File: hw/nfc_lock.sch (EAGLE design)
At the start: 10 parts, among them IC1 STM8S003F3, IC3 MCP170312MB, U1 M24SR16-YMN6T/2, X1 MINI-USB-32005-301

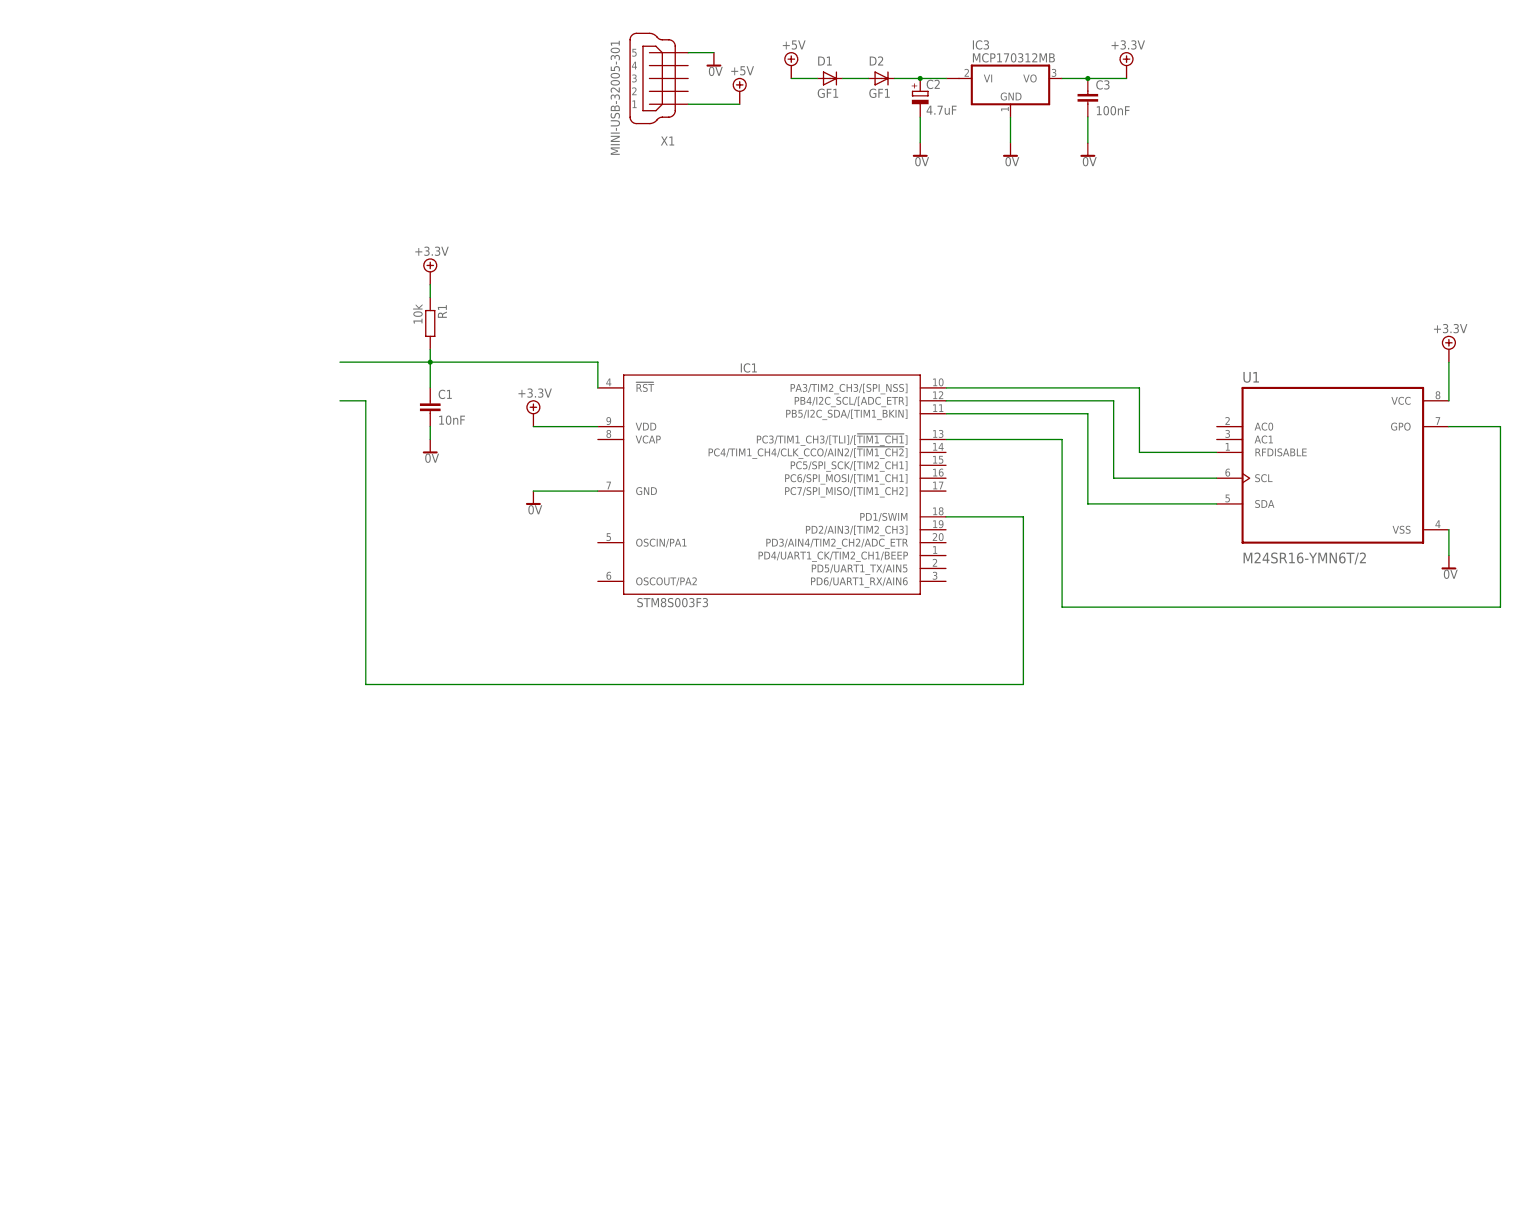
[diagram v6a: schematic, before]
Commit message: 2x n-mosfet for PWM of servos
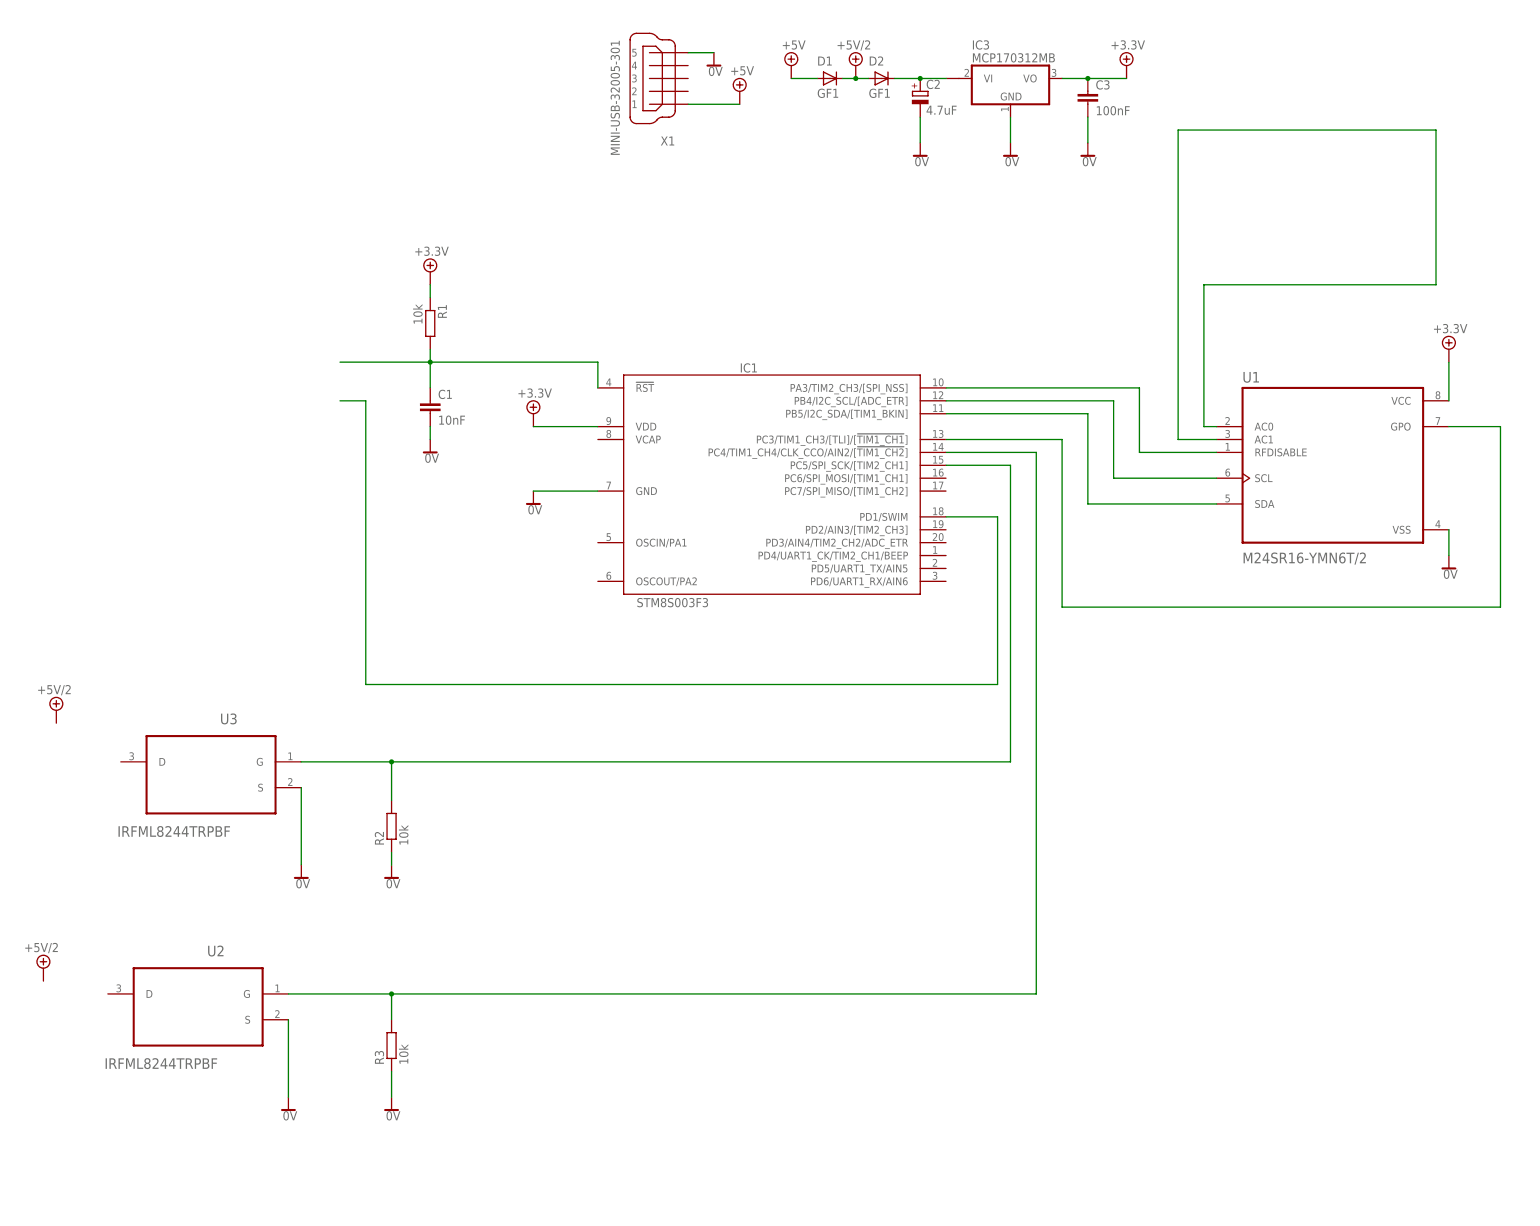
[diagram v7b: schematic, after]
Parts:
- added R2, R3: 10k, rcl:R-EU_R0805
- added U2, U3: IRFML8244TRPBF, irfml8244trpbf:IRFML8244TRPBF
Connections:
- net N$3 renamed +5V/2
- new net N$10: U1.AC0, U1.AC1
- new net N$13: IC1.PC5/SPI_SCK/[TIM2_CH1], R2.2, U3.G
- new net N$3: IC1.PC4/TIM1_CH4/CLK_CCO/AIN2/[!TIM1_CH2!], R3.2, U2.G
- net 0V: now also R2.1, R3.1, U2.S, U3.S
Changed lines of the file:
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@@
 <part name="SUPPLY12" library="supply2" deviceset="+5V/1" device="" value="+3.3V"/>
 <part name="SUPPLY13" library="supply2" deviceset="0V" device=""/>
+<part name="U3" library="irfml8244trpbf" deviceset="IRFML8244TRPBF" device=""/>
+<part name="SUPPLY14" library="supply2" deviceset="0V" device=""/>
+<part name="SUPPLY15" library="supply2" deviceset="+5V/2" device=""/>
+<part name="SUPPLY16" library="supply2" deviceset="+5V/2" device=""/>
+<part name="R2" library="rcl" deviceset="R-EU_" device="R0805" value="10k"/>
+<part name="SUPPLY17" library="supply2" deviceset="0V" device=""/>
+<part name="U2" library="irfml8244trpbf" deviceset="IRFML8244TRPBF" device=""/>
+<part name="R3" library="rcl" deviceset="R-EU_" device="R0805" value="10k"/>
+<part name="SUPPLY18" library="supply2" deviceset="0V" device=""/>
+<part name="SUPPLY19" library="supply2" deviceset="0V" device=""/>
+<part name="SUPPLY20" library="supply2" deviceset="+5V/2" device=""/>
 </parts>
 <sheets>
@@
 <instance part="SUPPLY12" gate="G$1" x="-43.18" y="116.84"/>
 <instance part="SUPPLY13" gate="0V" x="-43.18" y="81.28"/>
+<instance part="U3" gate="A" x="-86.36" y="20.32" rot="MR0"/>
+<instance part="SUPPLY14" gate="0V" x="-68.58" y="-2.54"/>
+<instance part="SUPPLY15" gate="G$1" x="40.64" y="157.48"/>
+<instance part="SUPPLY16" gate="G$1" x="-116.84" y="30.48"/>
+<instance part="R2" gate="G$1" x="-50.8" y="7.62" rot="R90"/>
+<instance part="SUPPLY17" gate="0V" x="-50.8" y="-2.54"/>
+<instance part="U2" gate="A" x="-88.9" y="-25.4" rot="MR0"/>
+<instance part="R3" gate="G$1" x="-50.8" y="-35.56" rot="R90"/>
+<instance part="SUPPLY18" gate="0V" x="-71.12" y="-48.26"/>
+<instance part="SUPPLY19" gate="0V" x="-50.8" y="-48.26"/>
+<instance part="SUPPLY20" gate="G$1" x="-119.38" y="-20.32"/>
 </instances>
 <busses>
@@
 <pinref part="SUPPLY13" gate="0V" pin="0V"/>
 <wire x1="-43.18" y1="83.82" x2="-43.18" y2="86.36" width="0.1524" layer="91"/>
+</segment>
+<segment>
+<pinref part="U3" gate="A" pin="S"/>
+<pinref part="SUPPLY14" gate="0V" pin="0V"/>
+<wire x1="-68.58" y1="15.24" x2="-68.58" y2="0" width="0.1524" layer="91"/>
+</segment>
+<segment>
+<pinref part="R2" gate="G$1" pin="1"/>
+<pinref part="SUPPLY17" gate="0V" pin="0V"/>
+<wire x1="-50.8" y1="2.54" x2="-50.8" y2="0" width="0.1524" layer="91"/>
+</segment>
+<segment>
+<pinref part="U2" gate="A" pin="S"/>
+<pinref part="SUPPLY18" gate="0V" pin="0V"/>
+<wire x1="-71.12" y1="-45.72" x2="-71.12" y2="-30.48" width="0.1524" layer="91"/>
+</segment>
+<segment>
+<pinref part="R3" gate="G$1" pin="1"/>
+<pinref part="SUPPLY19" gate="0V" pin="0V"/>
+<wire x1="-50.8" y1="-45.72" x2="-50.8" y2="-40.64" width="0.1524" layer="91"/>
 </segment>
 </net>
@@
 <pinref part="SUPPLY7" gate="+5V" pin="+5V"/>
 <wire x1="17.78" y1="149.86" x2="7.62" y2="149.86" width="0.1524" layer="91"/>
-</segment>
-</net>
-<net name="N$3" class="0">
-<segment>
-<pinref part="D1" gate="D" pin="C"/>
-<pinref part="D2" gate="D" pin="A"/>
-<wire x1="43.18" y1="154.94" x2="38.1" y2="154.94" width="0.1524" layer="91"/>
 </segment>
 </net>
@@
 <segment>
 <pinref part="IC1" gate="G$1" pin="PD1/SWIM"/>
-<wire x1="58.42" y1="68.58" x2="73.66" y2="68.58" width="0.1524" layer="91"/>
-<wire x1="73.66" y1="68.58" x2="73.66" y2="35.56" width="0.1524" layer="91"/>
-<wire x1="73.66" y1="35.56" x2="-55.88" y2="35.56" width="0.1524" layer="91"/>
+<wire x1="58.42" y1="68.58" x2="68.58" y2="68.58" width="0.1524" layer="91"/>
+<wire x1="68.58" y1="68.58" x2="68.58" y2="35.56" width="0.1524" layer="91"/>
+<wire x1="68.58" y1="35.56" x2="-55.88" y2="35.56" width="0.1524" layer="91"/>
 <wire x1="-55.88" y1="35.56" x2="-55.88" y2="91.44" width="0.1524" layer="91"/>
 <wire x1="-55.88" y1="91.44" x2="-60.96" y2="91.44" width="0.1524" layer="91"/>
@@
 </segment>
 </net>
+<net name="+5V/2" class="0">
+<segment>
+<pinref part="D1" gate="D" pin="C"/>
+<pinref part="D2" gate="D" pin="A"/>
+<wire x1="43.18" y1="154.94" x2="40.64" y2="154.94" width="0.1524" layer="91"/>
+<pinref part="SUPPLY15" gate="G$1" pin="+5V/2"/>
+<wire x1="40.64" y1="154.94" x2="38.1" y2="154.94" width="0.1524" layer="91"/>
+<junction x="40.64" y="154.94"/>
+</segment>
+</net>
+<net name="N$3" class="0">
+<segment>
+<pinref part="IC1" gate="G$1" pin="PC4/TIM1_CH4/CLK_CCO/AIN2/[!TIM1_CH2!]"/>
+<wire x1="58.42" y1="81.28" x2="76.2" y2="81.28" width="0.1524" layer="91"/>
+<wire x1="76.2" y1="81.28" x2="76.2" y2="-25.4" width="0.1524" layer="91"/>
+<pinref part="U2" gate="A" pin="G"/>
+<pinref part="R3" gate="G$1" pin="2"/>
+<wire x1="-50.8" y1="-30.48" x2="-50.8" y2="-25.4" width="0.1524" layer="91"/>
+<wire x1="-50.8" y1="-25.4" x2="-71.12" y2="-25.4" width="0.1524" layer="91"/>
+<wire x1="76.2" y1="-25.4" x2="-50.8" y2="-25.4" width="0.1524" layer="91"/>
+<junction x="-50.8" y="-25.4"/>
+</segment>
+</net>
+<net name="N$10" class="0">
+<segment>
+<pinref part="U1" gate="G$1" pin="AC1"/>
+<wire x1="111.76" y1="83.82" x2="104.14" y2="83.82" width="0.1524" layer="91"/>
+<wire x1="104.14" y1="83.82" x2="104.14" y2="144.78" width="0.1524" layer="91"/>
+<wire x1="104.14" y1="144.78" x2="154.94" y2="144.78" width="0.1524" layer="91"/>
+<wire x1="154.94" y1="144.78" x2="154.94" y2="114.3" width="0.1524" layer="91"/>
+<wire x1="154.94" y1="114.3" x2="109.22" y2="114.3" width="0.1524" layer="91"/>
+<wire x1="109.22" y1="114.3" x2="109.22" y2="86.36" width="0.1524" layer="91"/>
+<pinref part="U1" gate="G$1" pin="AC0"/>
+<wire x1="109.22" y1="86.36" x2="111.76" y2="86.36" width="0.1524" layer="91"/>
+</segment>
+</net>
+<net name="N$13" class="0">
+<segment>
+<pinref part="U3" gate="A" pin="G"/>
+<pinref part="R2" gate="G$1" pin="2"/>
+<wire x1="-50.8" y1="12.7" x2="-50.8" y2="20.32" width="0.1524" layer="91"/>
+<wire x1="-50.8" y1="20.32" x2="-68.58" y2="20.32" width="0.1524" layer="91"/>
+<pinref part="IC1" gate="G$1" pin="PC5/SPI_SCK/[TIM2_CH1]"/>
+<wire x1="58.42" y1="78.74" x2="71.12" y2="78.74" width="0.1524" layer="91"/>
+<wire x1="71.12" y1="78.74" x2="71.12" y2="20.32" width="0.1524" layer="91"/>
+<wire x1="-50.8" y1="20.32" x2="71.12" y2="20.32" width="0.1524" layer="91"/>
+<junction x="-50.8" y="20.32"/>
+</segment>
+</net>

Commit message: added SWIM, connections to servos, signalling LED
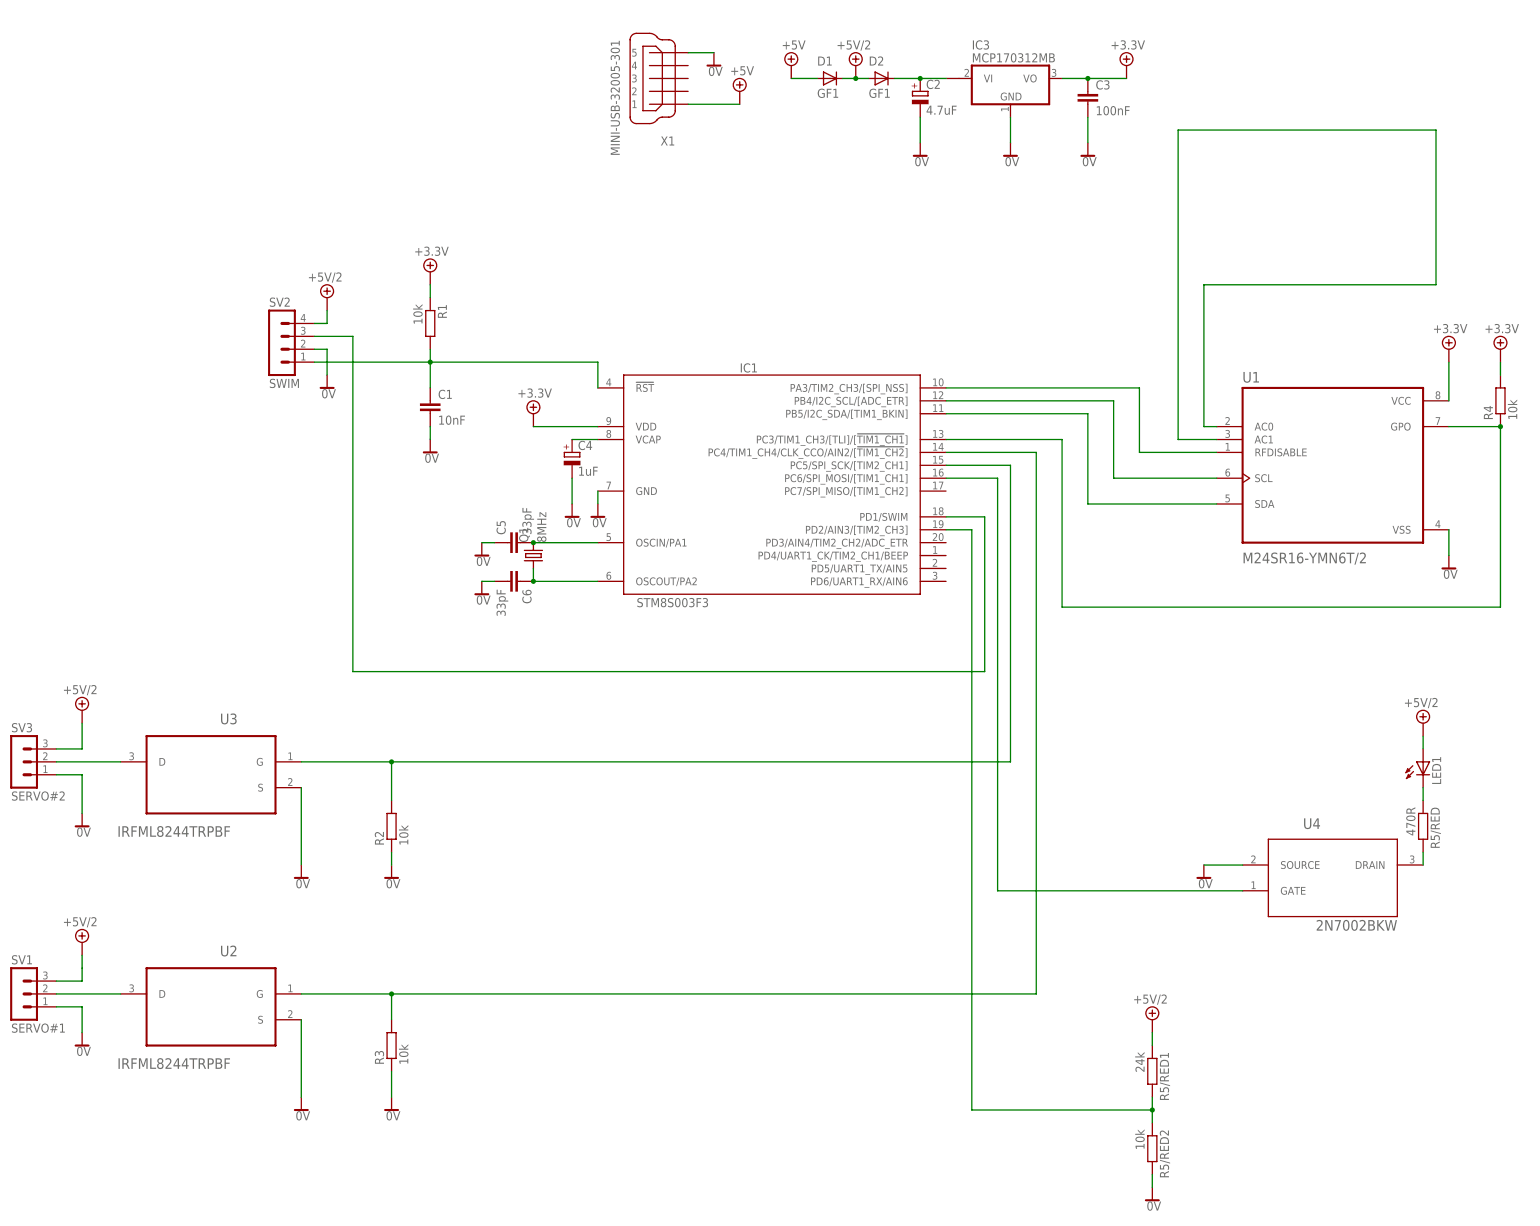
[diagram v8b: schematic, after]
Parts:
- added C4: 1uF, rcl:CPOL-EU153CLV-0405
- added C5, C6: 33pF, rcl:C-EUC1206
- added LED1: (no value), led:LEDCHIP-LED0603
- added Q1: 8MHz, crystal:CRYSTALSM49
- added R4, R5/RED2: 10k, rcl:R-EU_R0805
- added R5/RED: 470R, rcl:R-EU_R0805
- added R5/RED1: 24k, rcl:R-EU_R0805
- added SV1: SERVO#1, con-lstb:MA03-1
- added SV2: SWIM, con-lstb:MA04-1
- added SV3: SERVO#2, con-lstb:MA03-1
- added U4: 2N7002BKW, 2n7002:2N7002BKW
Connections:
- net N$10 renamed ANTENA
- new net N$11: SV3.2, U3.D
- new net N$12: LED1.C, R5/RED.1
- new net N$14: R5/RED.2, U4.DRAIN
- new net N$15: C4.+, IC1.VCAP
- new net N$16: C5.2, IC1.OSCIN/PA1, Q1.2
- new net N$17: C6.1, IC1.OSCOUT/PA2, Q1.1
- new net N$18: IC1.PD2/AIN3/[TIM2_CH3], R5/RED1.2, R5/RED2.1
- new net N$19: IC1.PC6/SPI_MOSI/[TIM1_CH1], U4.GATE
- new net N$9: SV1.2, U2.D
- net +5V/1: now also R4.2
- net +5V/2: now also LED1.A, R5/RED1.1, SV1.3, SV2.4, SV3.3
- net 0V: now also C4.-, C5.1, C6.2, R5/RED2.2, SV1.1, SV2.2, SV3.1, U4.SOURCE
- net N$5: now also SV2.1
- net N$6: now also SV2.3
- net N$8: now also R4.1
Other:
- moved on the sheet: U2
